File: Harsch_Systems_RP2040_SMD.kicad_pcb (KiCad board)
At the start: 2 copper layers, 90.2 x 69.5 mm, 159 parts, among them J1 Jack-DC, J3 Conn_01x08_Female, J4 Conn_01x08_Female, J5 Conn_01x04_Female, J6 Conn_01x06_Female, J7 USB_A, Q1 BSS123, Q2 BSS123, Q3 BSS123, Q4 BSS123, Q5 BCP56, Q6 BCP56, Q7 BCP56, Q8 BCP56, SW1 SW_MEC_5E, U1 XC6210B332MR, U10 TLV9304IDR, U11 TPS56339DDC, U3 RP2040, U4 W25Q32JVSSIQ_TR, U5 TLV9004xRUCR, U6 ELQ3H7, U7 TLV9004xRUCR, U8 ELQ3H7, U9 ELQ3H7, Y1 12MHz

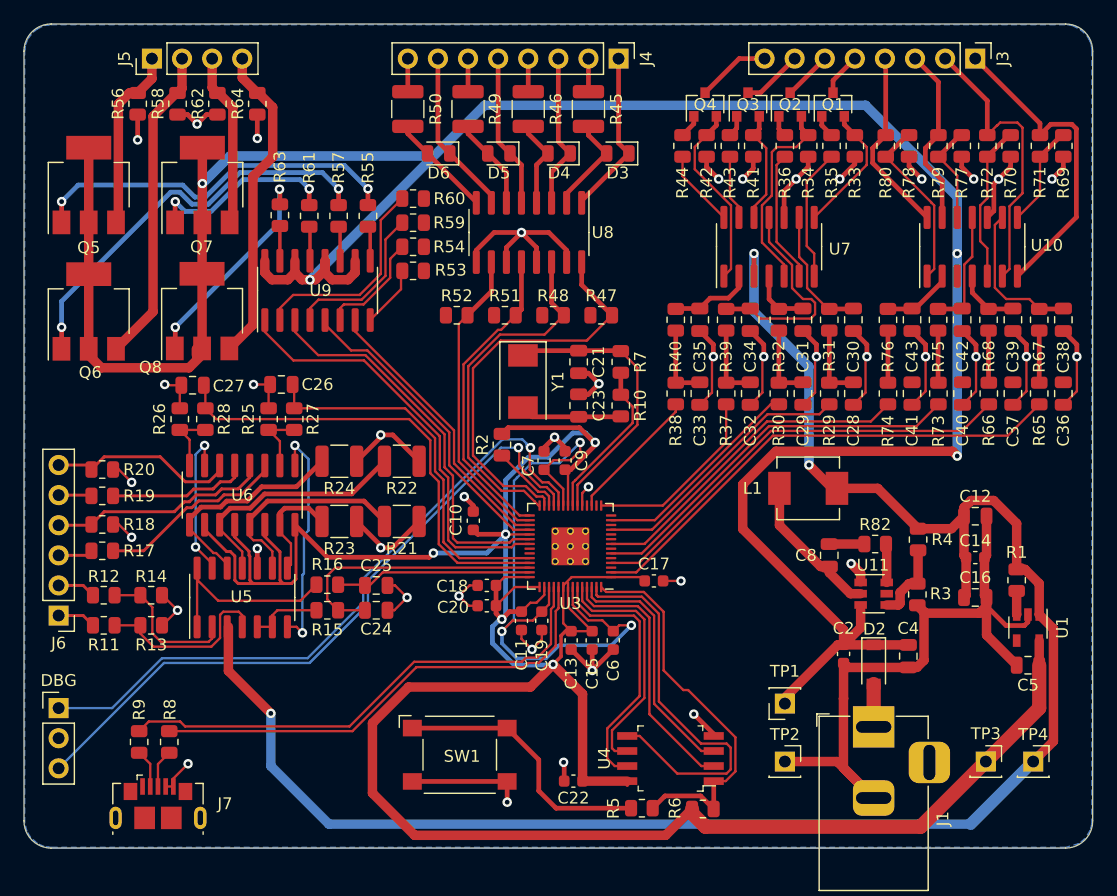
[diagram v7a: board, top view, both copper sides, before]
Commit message: Re-added mounting holes, fixed a small issue
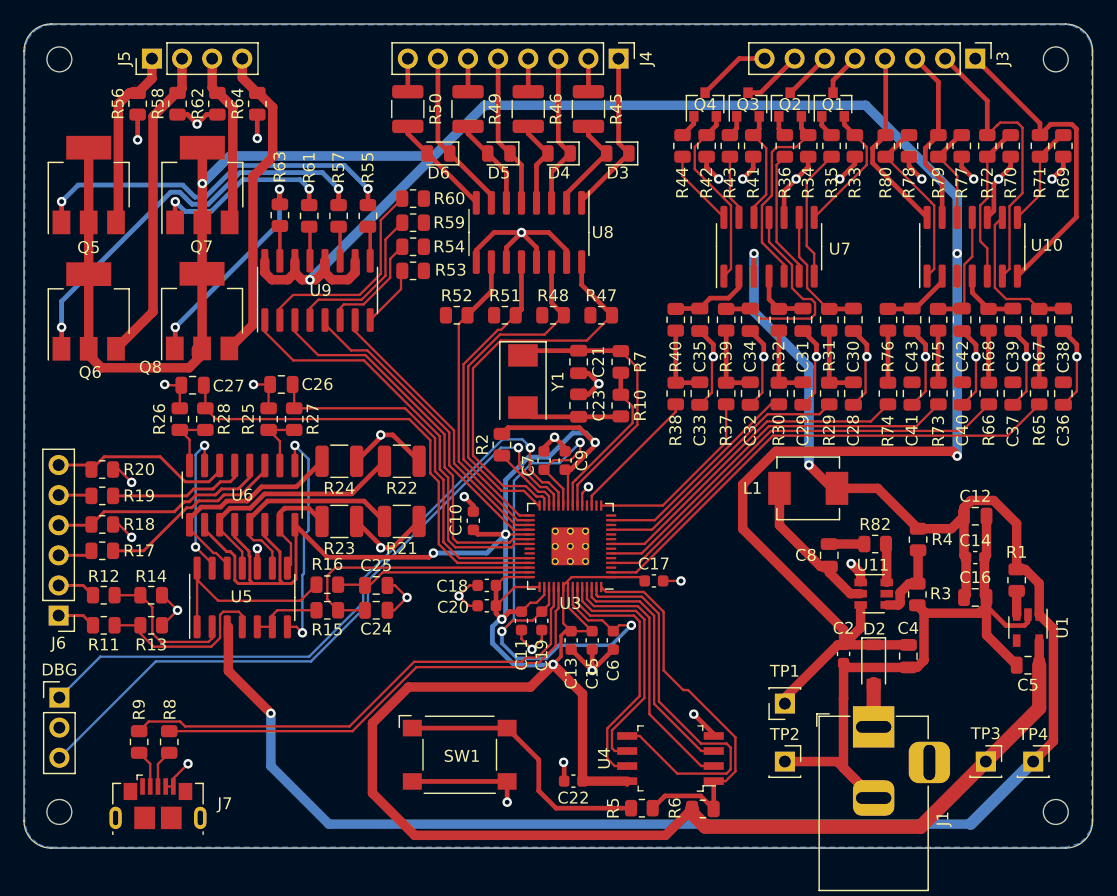
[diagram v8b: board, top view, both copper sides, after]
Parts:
- added REF**: MountingHole_2.1mm, MountingHole:MountingHole_2.1mm, F.Cu at (93.5, 57.4)
- added REF**: MountingHole_2.1mm, MountingHole:MountingHole_2.1mm, F.Cu at (177.5, 57.4)
- added REF**: MountingHole_2.1mm, MountingHole:MountingHole_2.1mm, F.Cu at (177.5, 120.9)
- added REF**: MountingHole_2.1mm, MountingHole:MountingHole_2.1mm, F.Cu at (93.5, 120.9)
- moved DBG 0.89 mm to (93.5, 111.3)
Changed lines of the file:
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@@
     (thickness 1.6)
     (drawings 8)
-    (tracks 1207)
+    (tracks 1206)
     (zones 0)
-    (modules 159)
+    (modules 163)
     (nets 151)
   )
@@
   )
   (setup
-    (last_trace_width 0.8)
+    (last_trace_width 0.2)
     (user_trace_width 0.2)
     (user_trace_width 0.25)
@@
     (add_net /ADC3)
   )
+  (module MountingHole:MountingHole_2.1mm (layer F.Cu)
+    (at 93.472 57.404)
+    (descr "Mounting Hole 2.1mm, no annular")
+    (tags "mounting hole 2.1mm no annular")
+    (attr virtual)
+    (fp_text reference REF** (at 0.508 -1.778) (layer F.SilkS) hide
+      (effects (font (size 1 1) (thickness 0.15)))
+    )
+    (fp_text value MountingHole_2.1mm (at 0 3.2) (layer F.Fab)
+      (effects (font (size 1 1) (thickness 0.15)))
+    )
+    (fp_circle (center 0 0) (end 2.1 0) (layer Cmts.User) (width 0.15))
+    (fp_circle (center 0 0) (end 2.35 0) (layer F.CrtYd) (width 0.05))
+    (fp_text user %R (at 0.3 0) (layer F.Fab)
+      (effects (font (size 1 1) (thickness 0.15)))
+    )
+    (pad "" np_thru_hole circle (at 0 0) (size 2.1 2.1) (drill 2.1) (layers *.Cu *.Mask))
+  )
+  (module MountingHole:MountingHole_2.1mm (layer F.Cu)
+    (at 177.546 57.404)
+    (descr "Mounting Hole 2.1mm, no annular")
+    (tags "mounting hole 2.1mm no annular")
+    (attr virtual)
+    (fp_text reference REF** (at 0.508 -1.778) (layer F.SilkS) hide
+      (effects (font (size 1 1) (thickness 0.15)))
+    )
+    (fp_text value MountingHole_2.1mm (at 0 3.2) (layer F.Fab)
+      (effects (font (size 1 1) (thickness 0.15)))
+    )
+    (fp_circle (center 0 0) (end 2.1 0) (layer Cmts.User) (width 0.15))
+    (fp_circle (center 0 0) (end 2.35 0) (layer F.CrtYd) (width 0.05))
+    (fp_text user %R (at 0.3 0) (layer F.Fab)
+      (effects (font (size 1 1) (thickness 0.15)))
+    )
+    (pad "" np_thru_hole circle (at 0 0) (size 2.1 2.1) (drill 2.1) (layers *.Cu *.Mask))
+  )
+  (module MountingHole:MountingHole_2.1mm (layer F.Cu)
+    (at 177.546 120.904)
+    (descr "Mounting Hole 2.1mm, no annular")
+    (tags "mounting hole 2.1mm no annular")
+    (attr virtual)
+    (fp_text reference REF** (at 0.508 -1.778) (layer F.SilkS) hide
+      (effects (font (size 1 1) (thickness 0.15)))
+    )
+    (fp_text value MountingHole_2.1mm (at 0 3.2) (layer F.Fab)
+      (effects (font (size 1 1) (thickness 0.15)))
+    )
+    (fp_circle (center 0 0) (end 2.1 0) (layer Cmts.User) (width 0.15))
+    (fp_circle (center 0 0) (end 2.35 0) (layer F.CrtYd) (width 0.05))
+    (fp_text user %R (at 0.3 0) (layer F.Fab)
+      (effects (font (size 1 1) (thickness 0.15)))
+    )
+    (pad "" np_thru_hole circle (at 0 0) (size 2.1 2.1) (drill 2.1) (layers *.Cu *.Mask))
+  )
+  (module MountingHole:MountingHole_2.1mm (layer F.Cu)
+    (at 93.472 120.904)
+    (descr "Mounting Hole 2.1mm, no annular")
+    (tags "mounting hole 2.1mm no annular")
+    (attr virtual)
+    (fp_text reference REF** (at 0.508 -1.778) (layer F.SilkS) hide
+      (effects (font (size 1 1) (thickness 0.15)))
+    )
+    (fp_text value MountingHole_2.1mm (at 0 3.2) (layer F.Fab)
+      (effects (font (size 1 1) (thickness 0.15)))
+    )
+    (fp_text user %R (at 0.3 0) (layer F.Fab)
+      (effects (font (size 1 1) (thickness 0.15)))
+    )
+    (fp_circle (center 0 0) (end 2.1 0) (layer Cmts.User) (width 0.15))
+    (fp_circle (center 0 0) (end 2.35 0) (layer F.CrtYd) (width 0.05))
+    (pad "" np_thru_hole circle (at 0 0) (size 2.1 2.1) (drill 2.1) (layers *.Cu *.Mask))
+  )
   (module Connector_BarrelJack:BarrelJack_Horizontal (layer F.Cu)
     (at 162.179 113.7285 90)
@@
   )
   (module Connector_PinHeader_2.54mm:PinHeader_1x03_P2.54mm_Vertical (layer F.Cu)
-    (at 93.4085 112.141)
+    (at 93.472 111.252)
     (descr "Through hole straight pin header, 1x03, 2.54mm pitch, single row")
     (tags "Through hole pin header THT 1x03 2.54mm single row")
@@
   (segment (start 137.1885 93.300532) (end 142.24302 88.246012) (width 0.2) (layer F.Cu) (net 4))
   (segment (start 162.179 113.7285) (end 162.179 110.10951) (width 1.2) (layer F.Cu) (net 15))
+  (segment (start 133.223 90.17) (end 133.0325 90.17) (width 0.2) (layer B.Cu) (net 20))
+  (segment (start 133.0325 90.17) (end 132.907001 90.044501) (width 0.2) (layer B.Cu) (net 20))
+  (segment (start 132.907001 90.044501) (end 132.907001 89.833999) (width 0.2) (layer B.Cu) (net 20))
+  (segment (start 132.907001 89.833999) (end 132.543 89.469999) (width 0.2) (layer B.Cu) (net 20))
   (segment (start 130.860801 89.469999) (end 119.10699 101.22381) (width 0.2) (layer B.Cu) (net 20))
   (segment (start 132.543 89.469999) (end 130.860801 89.469999) (width 0.2) (layer B.Cu) (net 20))
-  (segment (start 132.907001 89.833999) (end 132.543 89.469999) (width 0.2) (layer B.Cu) (net 20))
-  (segment (start 132.907001 90.044501) (end 132.907001 89.833999) (width 0.2) (layer B.Cu) (net 20))
-  (segment (start 133.0325 90.17) (end 132.907001 90.044501) (width 0.2) (layer B.Cu) (net 20))
-  (segment (start 133.223 90.17) (end 133.0325 90.17) (width 0.2) (layer B.Cu) (net 20))
-  (segment (start 119.10699 103.238348) (end 114.414348 107.93099) (width 0.2) (layer B.Cu) (net 20))
   (segment (start 119.10699 101.22381) (end 119.10699 103.238348) (width 0.2) (layer B.Cu) (net 20))
-  (segment (start 97.922801 112.141) (end 93.4085 112.141) (width 0.2) (layer B.Cu) (net 20))
-  (segment (start 102.132811 107.93099) (end 97.922801 112.141) (width 0.2) (layer B.Cu) (net 20))
-  (segment (start 114.414348 107.93099) (end 102.132811 107.93099) (width 0.2) (layer B.Cu) (net 20))
-  (segment (start 102.2985 108.331) (end 93.4085 117.221) (width 0.2) (layer B.Cu) (net 21))
-  (segment (start 114.580037 108.331) (end 102.2985 108.331) (width 0.2) (layer B.Cu) (net 21))
-  (segment (start 119.406037 103.505) (end 114.580037 108.331) (width 0.2) (layer B.Cu) (net 21))
+  (segment (start 96.92001 107.80399) (end 93.472 111.252) (width 0.2) (layer B.Cu) (net 20))
+  (segment (start 114.541348 107.80399) (end 96.92001 107.80399) (width 0.2) (layer B.Cu) (net 20))
+  (segment (start 119.10699 103.238348) (end 114.541348 107.80399) (width 0.2) (layer B.Cu) (net 20))
   (segment (start 119.507 103.505) (end 119.406037 103.505) (width 0.2) (layer B.Cu) (net 21))
   (segment (start 119.507 101.389498) (end 119.507 103.505) (width 0.2) (layer B.Cu) (net 21))
   (segment (start 130.726498 90.17) (end 119.507 101.389498) (width 0.2) (layer B.Cu) (net 21))
   (segment (start 132.207 90.17) (end 130.726498 90.17) (width 0.2) (layer B.Cu) (net 21))
+  (segment (start 119.406037 103.505) (end 114.707037 108.204) (width 0.2) (layer B.Cu) (net 21))
+  (segment (start 101.6 108.204) (end 93.472 116.332) (width 0.2) (layer B.Cu) (net 21))
+  (segment (start 114.707037 108.204) (end 101.6 108.204) (width 0.2) (layer B.Cu) (net 21))
   (segment (start 101.282499 59.031501) (end 100.076 60.238) (width 0.8) (layer F.Cu) (net 34))
   (segment (start 101.282499 57.3405) (end 101.282499 59.031501) (width 0.8) (layer F.Cu) (net 34))
